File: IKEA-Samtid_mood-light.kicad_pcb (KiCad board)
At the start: 2 copper layers, 100 x 100 mm, 154 parts, among them IC1 ATMEGA168PA-M, P1 FTDI, P2 POWER, P3.1 B-to-B-1A, P3.2 B-to-B-1B, P4.1 B-to-B-2A, P4.2 B-to-B-2B, Q1 BSS138, Q2 BSS138, SW1 ENTER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

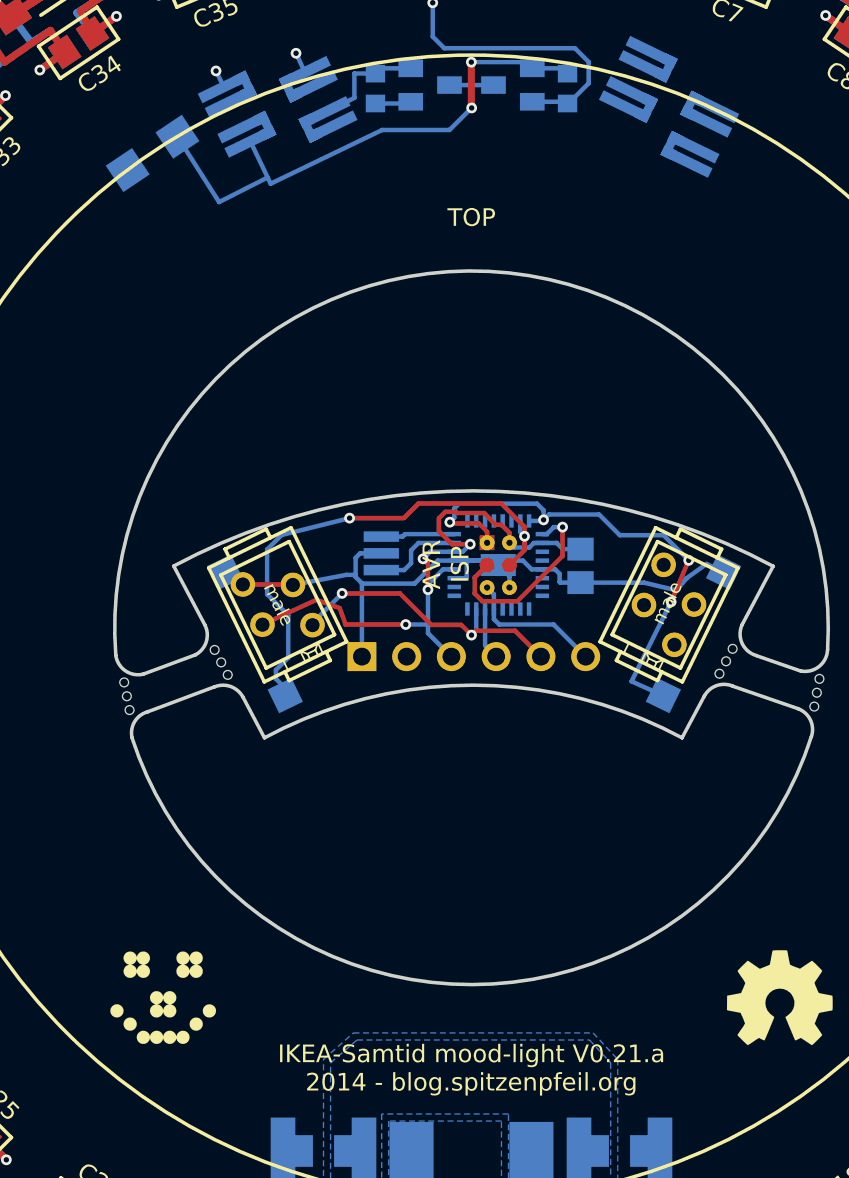
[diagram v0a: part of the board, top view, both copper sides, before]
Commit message: Moved DS2 to a much better place.
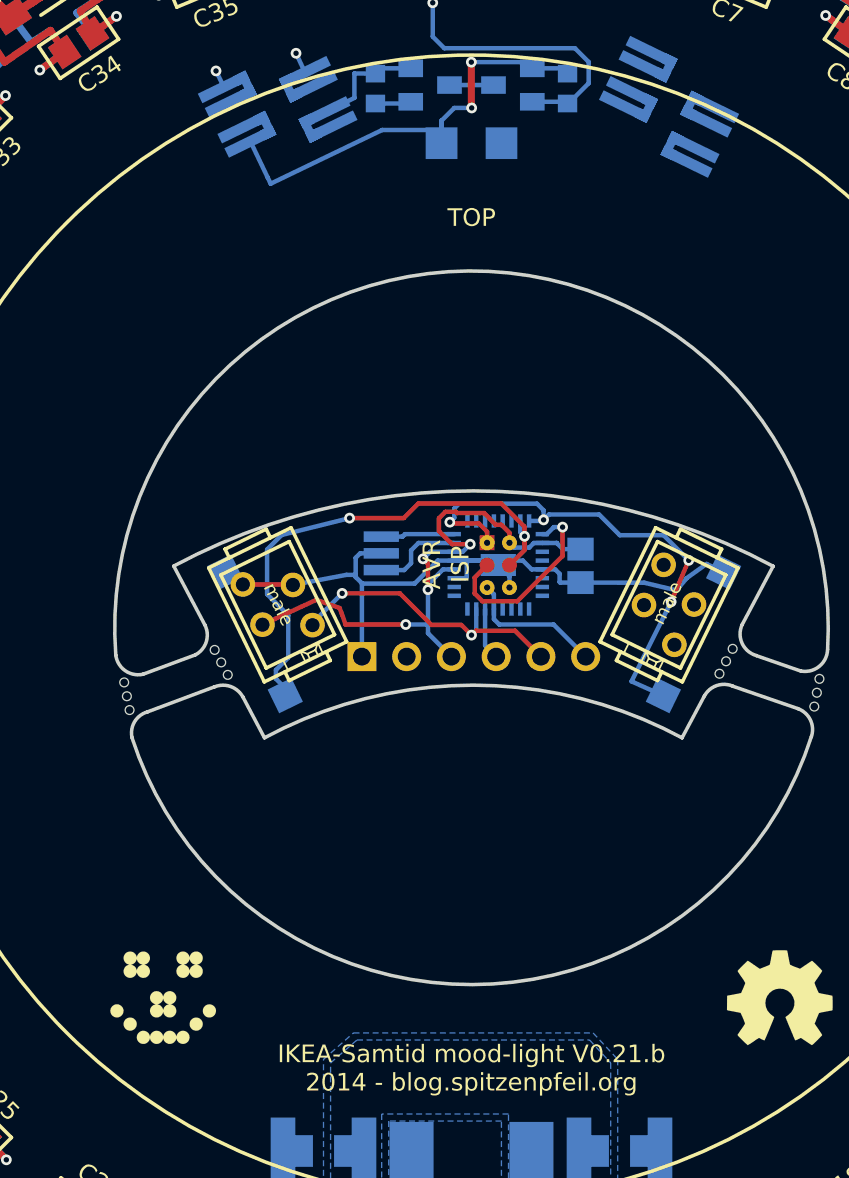
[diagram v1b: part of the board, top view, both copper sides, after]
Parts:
- moved DS2 18.1 mm to (150.0, 67.5), turned to 180 degrees
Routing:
- net /VCC.A: track 31.2 -> 25.3 mm
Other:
- board text added: "IKEA-Samtid mood-light V0.21.b 2014 - blog.spitzenpfeil.org"
- board text removed: "IKEA-Samtid mood-light V0.21.a 2014 - blog.spitzenpfeil.org"
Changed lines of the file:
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@@
     (thickness 1.6)
     (drawings 54)
-    (tracks 1422)
+    (tracks 1423)
     (zones 0)
     (modules 154)
@@
     (title IKEA-Samtid_mood-light)
     (date "24 Jul 2014")
-    (rev 0.21.a)
+    (rev 0.21.b)
     (company "2014 - blog.spitzenpfeil.org")
   )
@@
   )
   (setup
-    (last_trace_width 0.254)
+    (last_trace_width 0.4064)
     (user_trace_width 0.2032)
     (user_trace_width 0.254)
@@
     (pad_to_mask_clearance 0)
     (aux_axis_origin 0 0)
-    (visible_elements FFFCFF7F)
+    (visible_elements FFFFFF7F)
     (pcbplotparams
       (layerselection 402423809)
@@
   )
   (module my_parts:MADW__diode_sub-SMA (layer B.Cu)
-    (at 131.9 68.08 33.8)
-    (fp_text reference DS2 (at 0 1.95 33.8) (layer B.SilkS)
+    (at 150 67.5 180)
+    (fp_text reference DS2 (at -0.01 -1.78 180) (layer B.SilkS)
       (effects (font (size 1 1) (thickness 0.2)) (justify mirror))
     )
-    (fp_text value SS14L (at 0 -2.15 33.8) (layer B.SilkS) hide
+    (fp_text value SS14L (at 0 -2.15 180) (layer B.SilkS) hide
       (effects (font (size 1 1) (thickness 0.2)) (justify mirror))
     )
@@
     (fp_line (start 1.45 -0.95) (end -1.45 -0.95) (layer B.SilkS) (width 0.2))
     (fp_line (start -1.45 -0.95) (end -1.45 0.95) (layer B.SilkS) (width 0.2))
-    (pad 1 smd rect (at -1.7 0 33.8) (size 1.8 1.8) (layers B.Cu B.Paste B.Mask)
+    (pad 1 smd rect (at -1.7 0 180) (size 1.8 1.8) (layers B.Cu B.Paste B.Mask)
       (net 1 +5V))
-    (pad 2 smd rect (at 1.7 0 33.8) (size 1.8 1.8) (layers B.Cu B.Paste B.Mask)
+    (pad 2 smd rect (at 1.7 0 180) (size 1.8 1.8) (layers B.Cu B.Paste B.Mask)
       (net 76 /VCC.A))
   )
@@
     (effects (font (size 0.75 0.75) (thickness 0.1875)) (justify mirror))
   )
-  (gr_text "IKEA-Samtid mood-light V0.21.a\n2014 - blog.spitzenpfeil.org" (at 150 120) (layer F.SilkS)
+  (gr_text "IKEA-Samtid mood-light V0.21.b\n2014 - blog.spitzenpfeil.org" (at 150 120) (layer F.SilkS)
     (effects (font (size 1 1) (thickness 0.2)))
   )
@@
   (via (at 150.01 65.5) (size 0.6096) (layers F.Cu B.Cu) (net 76))
   (segment (start 150.01 65.5) (end 150 65.5) (width 0.254) (layer B.Cu) (net 76))
-  (segment (start 150 65.5) (end 148.75 66.75) (width 0.254) (layer B.Cu) (net 76))
-  (segment (start 144.931379 66.75) (end 138.6 69.8) (width 0.254) (layer B.Cu) (net 76))
-  (segment (start 144.931379 66.75) (end 148.75 66.75) (width 0.254) (layer B.Cu) (net 76))
-  (segment (start 138.430306 69.44583) (end 138.6 69.8) (width 0.254) (layer B.Cu) (net 76))
   (segment (start 149.99 62.9) (end 150.03 62.9) (width 0.254) (layer B.Cu) (net 76))
   (via (at 149.99 62.9) (size 0.6096) (layers F.Cu B.Cu) (net 76))
   (segment (start 149.99 65.48) (end 149.99 62.9) (width 0.4064) (layer F.Cu) (net 76))
-  (segment (start 138.430306 69.44583) (end 135.6741 70.84314) (width 0.254) (layer B.Cu) (net 76))
-  (segment (start 135.6741 70.84314) (end 133.312674 67.134297) (width 0.254) (layer B.Cu) (net 76))
   (segment (start 155.14836 63.25) (end 155.45 63.55164) (width 0.254) (layer B.Cu) (net 76) (status 30))
   (segment (start 153.45 63.25) (end 155.14836 63.25) (width 0.254) (layer B.Cu) (net 76) (status 30))
+  (segment (start 150.01 65.5) (end 149.02 65.5) (width 0.254) (layer B.Cu) (net 76))
+  (segment (start 148.3 66.22) (end 148.3 67.5) (width 0.254) (layer B.Cu) (net 76))
+  (segment (start 149.02 65.5) (end 148.3 66.22) (width 0.254) (layer B.Cu) (net 76))
+  (segment (start 144.931379 66.75) (end 148.3 66.75) (width 0.254) (layer B.Cu) (net 76))
+  (segment (start 138.6 69.8) (end 144.931379 66.75) (width 0.254) (layer B.Cu) (net 76))
+  (segment (start 138.430306 69.44583) (end 138.6 69.8) (width 0.254) (layer B.Cu) (net 76))
+  (segment (start 148.3 66.75) (end 148.3 66.22) (width 0.254) (layer B.Cu) (net 76))
   (segment (start 137.451154 67.397033) (end 138.430306 69.44583) (width 0.254) (layer B.Cu) (net 76))
   (segment (start 135.943157 64.305181) (end 135.5 63.4) (width 0.254) (layer B.Cu) (net 77))

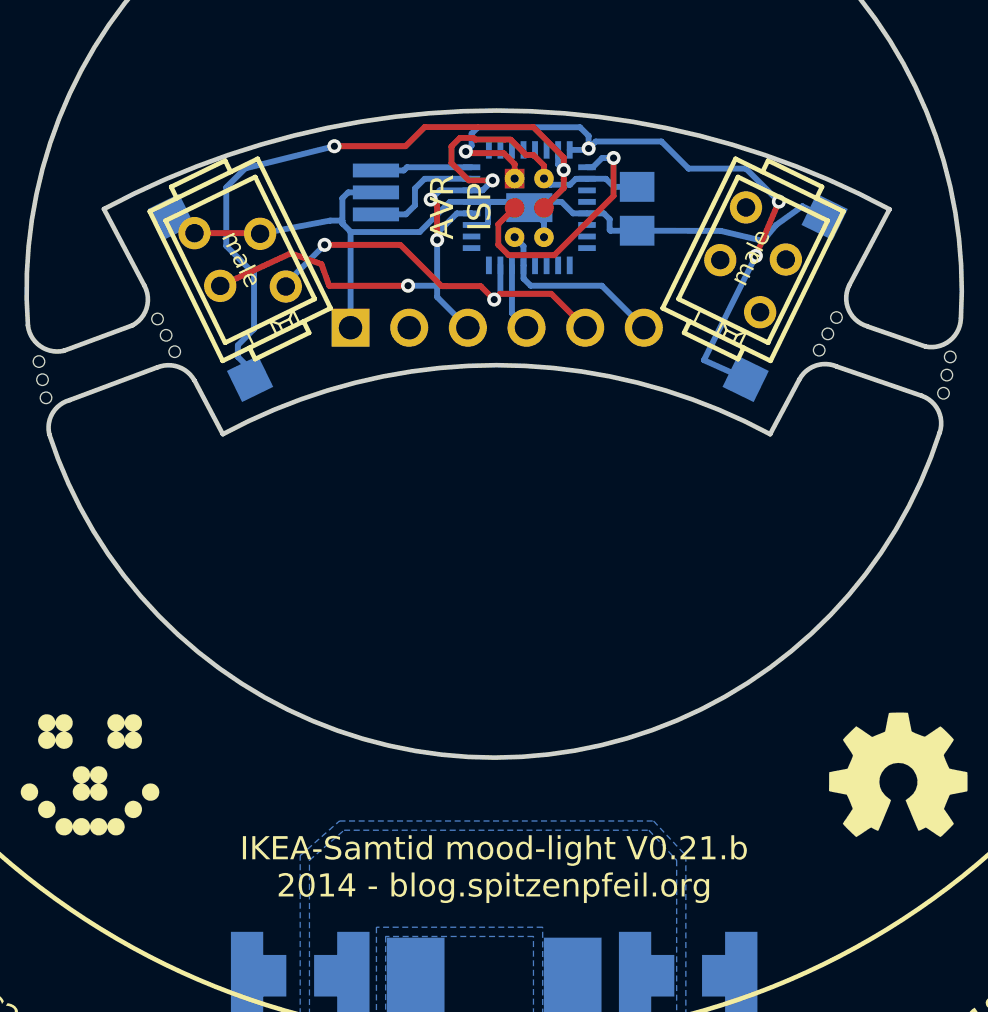
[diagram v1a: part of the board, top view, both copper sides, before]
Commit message: Added a status LED.
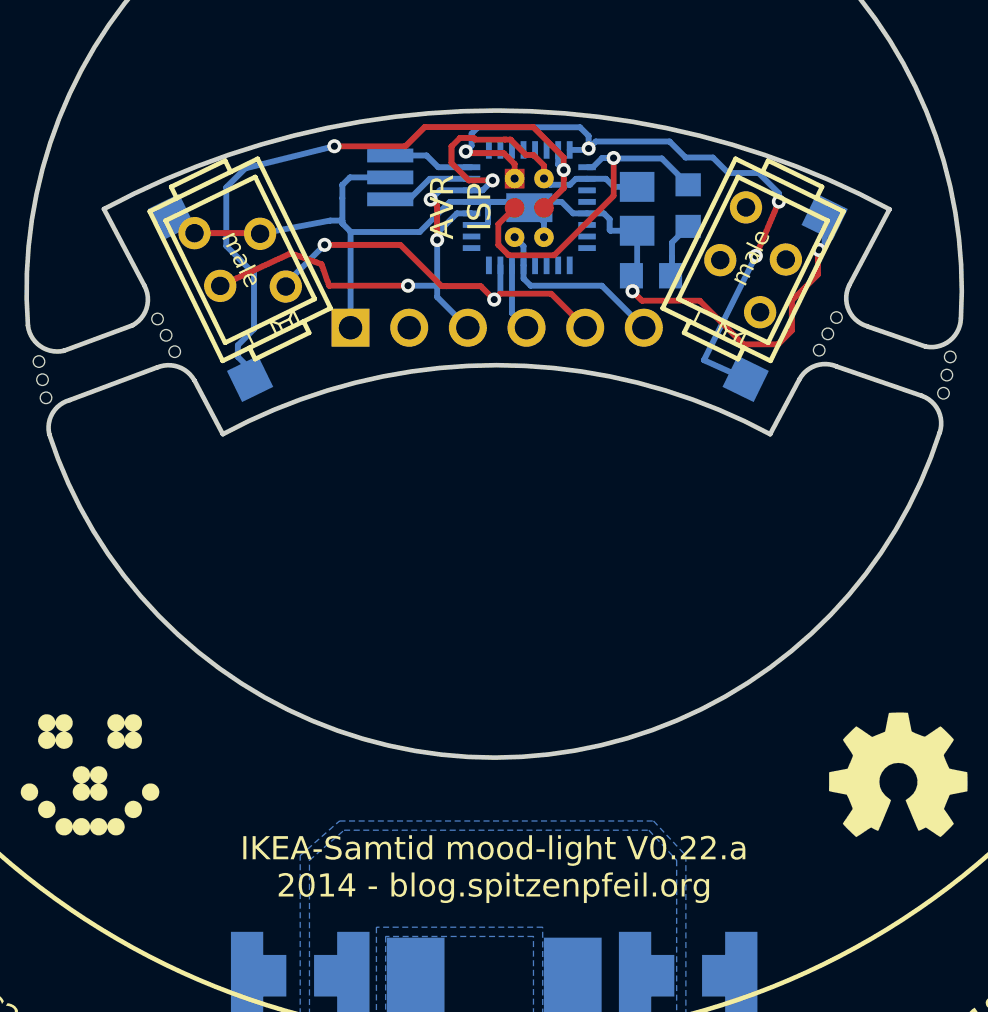
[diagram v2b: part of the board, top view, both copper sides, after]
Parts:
- added D65: LED, my_parts:MADW__CHIPLED-0603, B.Cu at (158.4, 91.3)
- added R1: 1k, my_parts:MADW__R0603_2, B.Cu at (156.8, 94.4)
- moved X1 0.90 mm to (145.5, 90.1)
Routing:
- net /GND.B: track 44.4 -> 53.1 mm, vias 0 -> 2
- net /SCK: track 11.1 -> 14.9 mm
- net Net-(D65-Pad2): track 0.00 -> 2.46 mm
- net /XTAL1: track 6.07 -> 5.48 mm
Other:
- board text added: "13"
- board text added: "IKEA-Samtid mood-light V0.22.a 2014 - blog.spitzenpfeil.org"
- board text removed: "IKEA-Samtid mood-light V0.21.b 2014 - blog.spitzenpfeil.org"

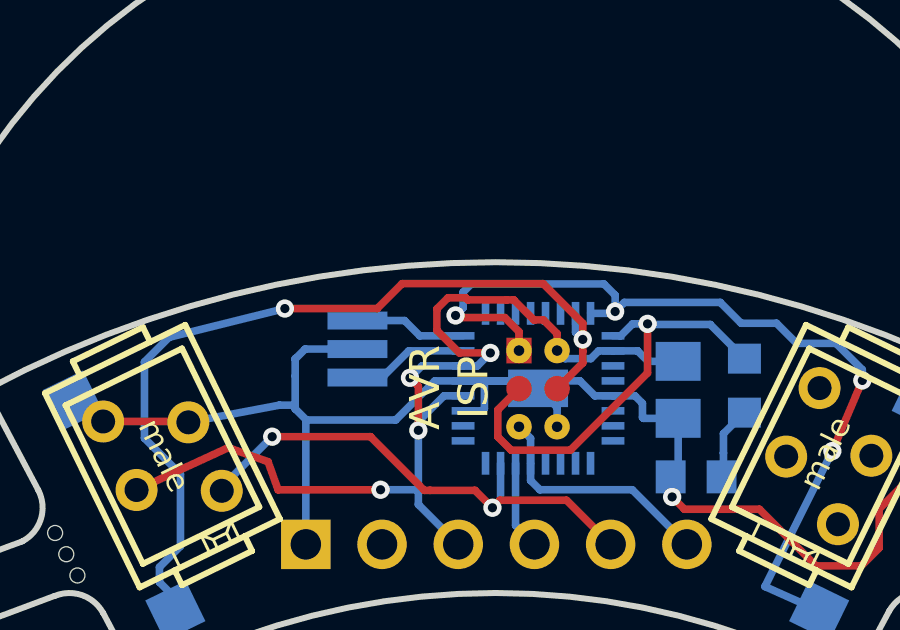
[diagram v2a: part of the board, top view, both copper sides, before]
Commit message: Tweaked some tracks around a via. Not enough clearance.
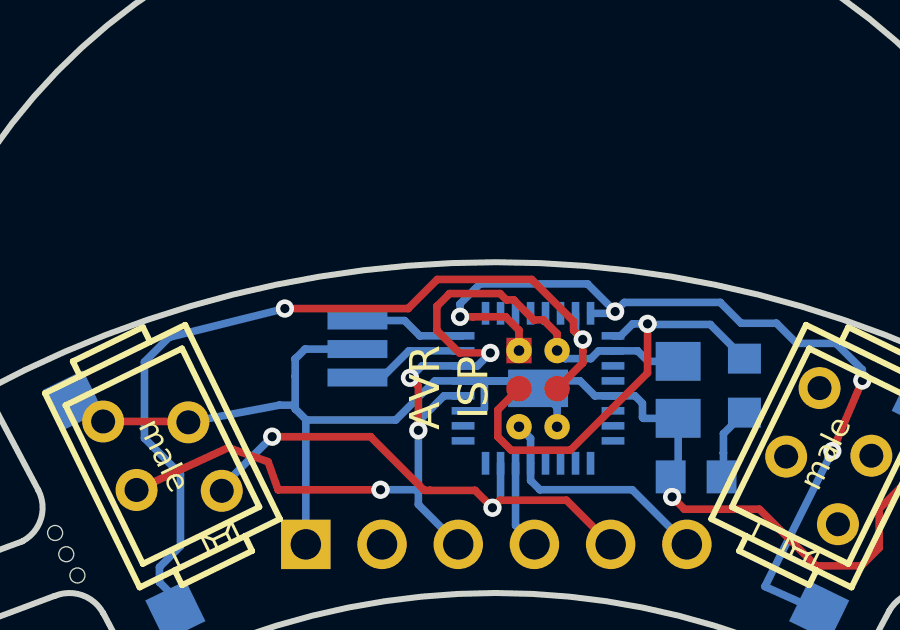
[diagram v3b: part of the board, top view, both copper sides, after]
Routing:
- net /MISO: track 29.8 -> 29.2 mm
